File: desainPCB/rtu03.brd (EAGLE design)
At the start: 74.9 x 74.6 mm, 13 parts, among them M1 ARDUINO-PRO-MINI-5.0V, X1 JST-XH-02-PIN-LONG-PAD

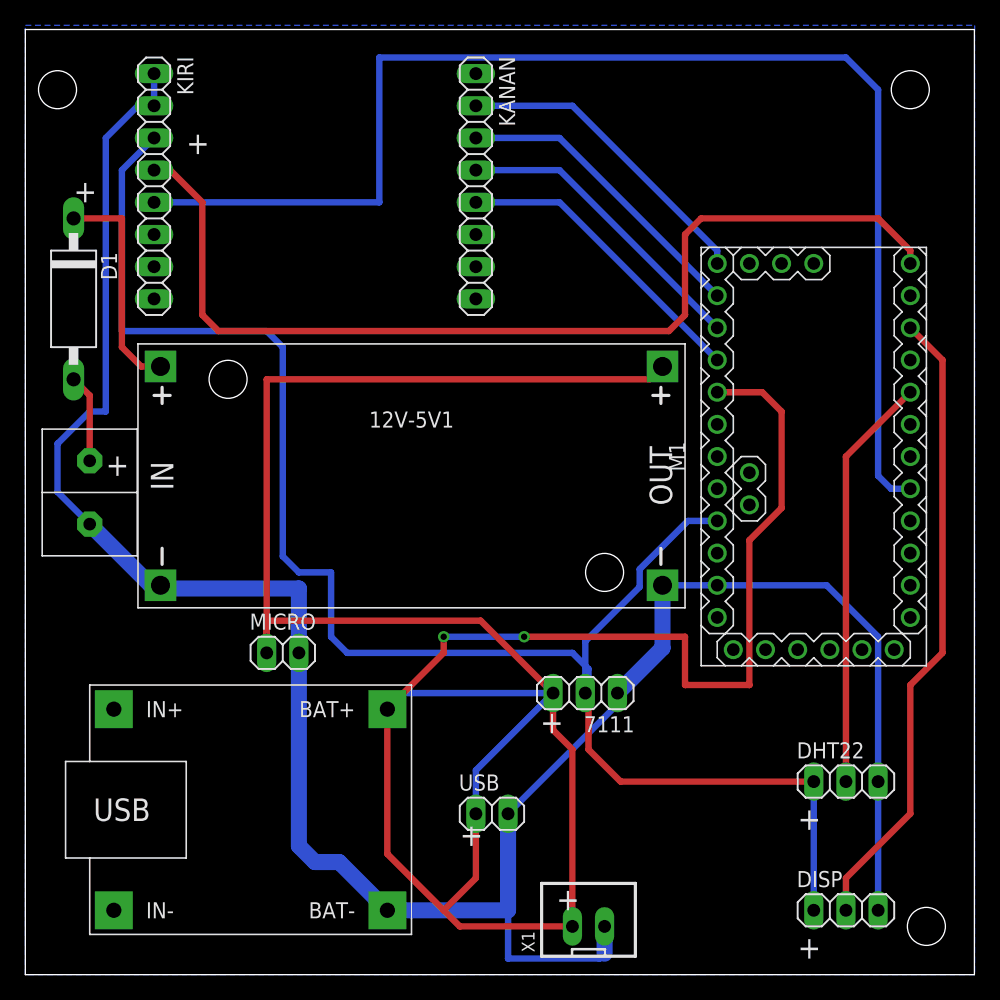
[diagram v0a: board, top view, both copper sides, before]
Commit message: new sensor suhu
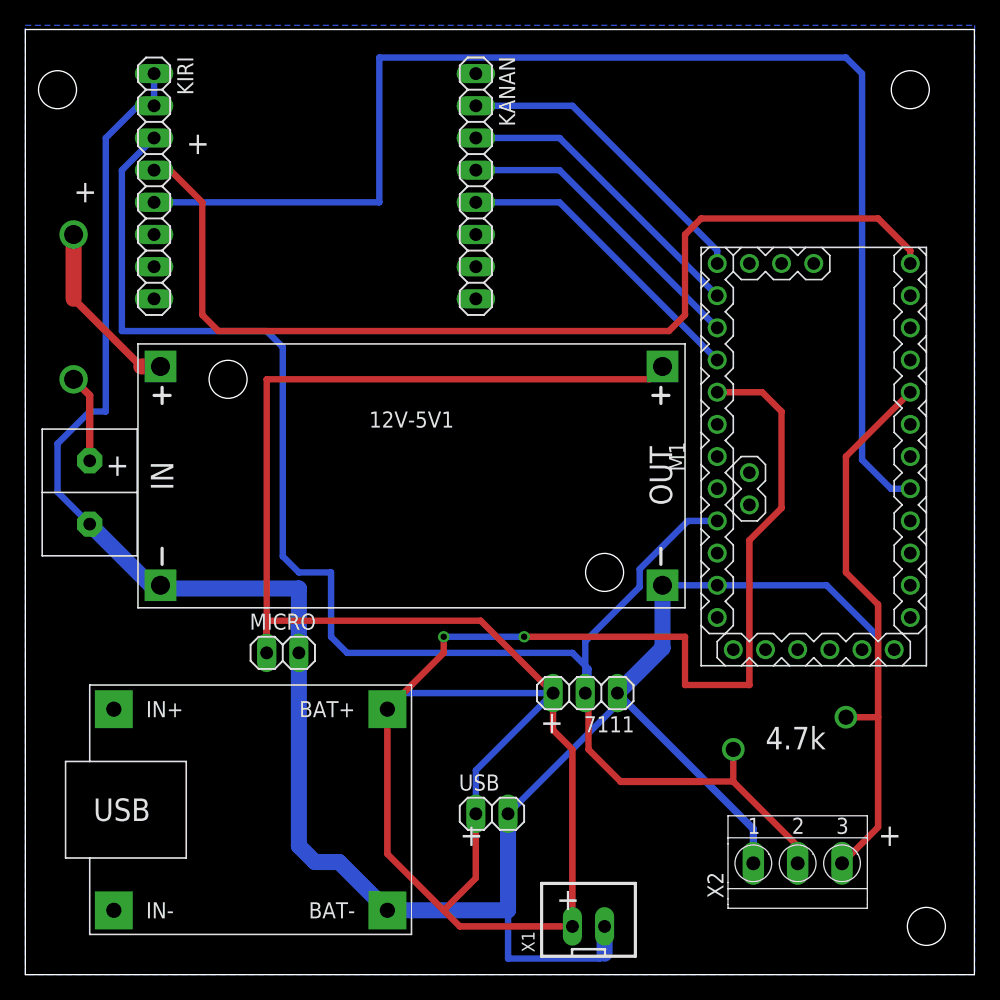
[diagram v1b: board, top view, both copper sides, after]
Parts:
- removed D1: 1N5060GP, diode:DO15-12
- removed DHT22, DISP: (no value), pinhead:1X03
- added X2: TERMINAL-BLOCK-3.5MM-3-PIN-LONG-PAD, Rembrandt Electronics - Terminal Block 3-5mm v1-0:TERMINAL-BLOCK-3-PIN-3.5MM-LONG-PAD
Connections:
- removed net 5: DHT22.2, M1.J7.5
- removed net N$1: D1.A, U$1.P1
- removed net N$2: 12V-5V1.IN+, D1.C
- new net IN+: U$1.P1
- new net OUT+: 12V-5V1.IN+
- net 3V: now also M1.J7.5, X2.2, X2.3; no longer DHT22.1, DISP.1
- net 7: no longer DISP.2
- net GND: now also X2.1; no longer DHT22.3, DISP.3
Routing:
- net 7: track 50.2 -> 0.00 mm
- net 3V: track 131.6 -> 170.4 mm, vias 0 -> 2
- net 5: track 32.8 -> 0.00 mm
- net N$2: track 17.6 -> 0.00 mm
- net OUT+: track 0.00 -> 14.1 mm, vias 0 -> 1
- net N$1: track 6.96 -> 0.00 mm
- net IN+: track 0.00 -> 6.96 mm, vias 0 -> 1
- net GND: track 183.5 -> 179.8 mm
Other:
- board text added: "4.7k"
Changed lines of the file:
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@@
 <text x="40.64" y="19.05" size="1.778" layer="21">+</text>
 <text x="6.35" y="39.37" size="1.778" layer="21">+</text>
-<text x="60.96" y="1.27" size="1.778" layer="21">+</text>
-<text x="60.96" y="11.43" size="1.778" layer="21">+</text>
+<text x="67.31" y="10.16" size="1.778" layer="21">+</text>
 <text x="41.91" y="5.08" size="1.778" layer="21">+</text>
 <text x="3.81" y="60.96" size="1.778" layer="21">+</text>
 <text x="12.7" y="64.77" size="1.778" layer="21">+</text>
+<text x="58.42" y="17.78" size="1.778" layer="21">4.7k</text>
 </plain>
 <attributes>
@@
 <element name="X1" library="Rembrandt Electronics - JST XH Connectors v1-0" package="JST-XH-02-PACKAGE-LONG-PAD" value="JST-XH-02-PIN-LONG-PAD" x="44.45" y="3.81" smashed="yes">
 <attribute name="NAME" x="40.195" y="1.77" size="1.016" layer="25" ratio="10" rot="R90"/>
-<attribute name="VALUE" x="41.1475" y="7.7025" size="1.016" layer="27" ratio="10"/>
 </element>
 <element name="KANAN" library="pinhead" library_urn="urn:adsk.eagle:library:325" package="1X08" package3d_urn="urn:adsk.eagle:package:22409/2" value="" x="35.56" y="62.23" smashed="yes" rot="R270">
@@
 <attribute name="VALUE" x="48.006" y="25.4" size="1.27" layer="27" rot="R180"/>
 </element>
-<element name="DHT22" library="pinhead" library_urn="urn:adsk.eagle:library:325" package="1X03" package3d_urn="urn:adsk.eagle:package:22458/2" value="" x="64.77" y="15.24" smashed="yes">
-<attribute name="NAME" x="60.8838" y="17.0688" size="1.27" layer="25" ratio="10"/>
-<attribute name="POPULARITY" value="92" x="64.77" y="15.24" size="1.778" layer="27" display="off"/>
-<attribute name="VALUE" x="60.96" y="12.065" size="1.27" layer="27"/>
-</element>
-<element name="DISP" library="pinhead" library_urn="urn:adsk.eagle:library:325" package="1X03" package3d_urn="urn:adsk.eagle:package:22458/2" value="" x="64.77" y="5.08" smashed="yes">
-<attribute name="NAME" x="60.8838" y="6.9088" size="1.27" layer="25" ratio="10"/>
-<attribute name="POPULARITY" value="92" x="64.77" y="5.08" size="1.778" layer="27" display="off"/>
-<attribute name="VALUE" x="60.96" y="1.905" size="1.27" layer="27"/>
-</element>
 <element name="U$2" library="diy-modules (1)" package="BATTERY-CHARGER-LI-5V" value="BATTERY-CHARGER-LI-5V" x="17.78" y="12.7" smashed="yes">
 <attribute name="VALUE" x="17.78" y="9.525" size="1.27" layer="27" align="top-center"/>
@@
 <attribute name="VALUE" x="34.29" y="9.525" size="1.27" layer="27"/>
 </element>
-<element name="D1" library="diode" library_urn="urn:adsk.eagle:library:210" package="DO15-12" package3d_urn="urn:adsk.eagle:package:43369/2" value="1N5060GP" x="3.81" y="53.34" smashed="yes" rot="R270">
-<attribute name="NAME" x="5.969" y="57.023" size="1.27" layer="25" ratio="10" rot="R270"/>
-<attribute name="POPULARITY" value="0" x="3.81" y="53.34" size="1.778" layer="27" rot="R270" display="off"/>
-<attribute name="VALUE" x="2.413" y="55.499" size="1.27" layer="27" ratio="10" rot="R270"/>
+<element name="X2" library="Rembrandt Electronics - Terminal Block 3-5mm v1-0" package="TERMINAL-BLOCK-3-PIN-3.5MM-LONG-PAD" value="TERMINAL-BLOCK-3.5MM-3-PIN-LONG-PAD" x="60.96" y="8.89" smashed="yes">
+<attribute name="NAME" x="55.105" y="6.0325" size="1.27" layer="25" rot="R90"/>
 </element>
 </elements>
@@
 <contactref element="KIRI" pad="2"/>
 <contactref element="7111" pad="1"/>
-<contactref element="DHT22" pad="3"/>
-<contactref element="DISP" pad="3"/>
 <contactref element="U$2" pad="BAT-"/>
 <contactref element="MICRO" pad="2"/>
@@
 <wire x1="45.339" y1="1.27" x2="38.1" y2="1.27" width="0.508" layer="16"/>
 <wire x1="38.1" y1="1.27" x2="38.1" y2="5.08" width="0.508" layer="16"/>
-<wire x1="67.31" y1="15.24" x2="67.31" y2="5.08" width="0.508" layer="16"/>
 <wire x1="50.292" y1="30.734" x2="54.61" y2="30.734" width="0.508" layer="16"/>
 <wire x1="54.61" y1="30.734" x2="63.246" y2="30.734" width="0.508" layer="16"/>
 <wire x1="63.246" y1="30.734" x2="67.31" y2="26.67" width="0.508" layer="16"/>
-<wire x1="67.31" y1="26.67" x2="67.31" y2="15.24" width="0.508" layer="16"/>
 <wire x1="10.16" y1="71.12" x2="10.16" y2="68.58" width="0.508" layer="16"/>
 <wire x1="5.08" y1="35.56" x2="2.54" y2="38.1" width="0.508" layer="16"/>
@@
 <vertex x="0" y="0"/>
 </polygon>
+<contactref element="X2" pad="1"/>
+<wire x1="46.736" y1="22.225" x2="57.46" y2="11.501" width="0.58" layer="16"/>
+<wire x1="57.46" y1="11.501" x2="57.46" y2="8.79" width="0.58" layer="16"/>
 </signal>
 <signal name="3V">
 <contactref element="KIRI" pad="3"/>
 <contactref element="7111" pad="2"/>
-<contactref element="DHT22" pad="1"/>
-<contactref element="DISP" pad="1"/>
-<wire x1="62.23" y1="15.24" x2="62.23" y2="5.08" width="0.508" layer="16"/>
 <wire x1="10.16" y1="66.04" x2="7.62" y2="63.5" width="0.508" layer="16"/>
 <wire x1="7.62" y1="63.5" x2="7.62" y2="50.8" width="0.508" layer="16"/>
@@
 <wire x1="44.45" y1="21.971" x2="44.45" y2="17.78" width="0.508" layer="1"/>
 <wire x1="44.45" y1="17.78" x2="46.99" y2="15.24" width="0.508" layer="1"/>
-<wire x1="46.99" y1="15.24" x2="62.23" y2="15.24" width="0.508" layer="1"/>
 <contactref element="M1" pad="J6.4"/>
 <wire x1="44.196" y1="22.225" x2="44.196" y2="26.308625" width="0.508" layer="16"/>
@@
 <wire x1="44.196" y1="26.308625" x2="48.49" y2="30.602625" width="0.508" layer="16"/>
 <wire x1="48.49" y1="30.602625" x2="48.49" y2="32.0067375" width="0.508" layer="16"/>
+<contactref element="X2" pad="3"/>
+<contactref element="X2" pad="2"/>
+<contactref element="M1" pad="J7.5"/>
+<wire x1="69.85" y1="45.974" x2="64.77" y2="40.894" width="0.508" layer="1"/>
+<wire x1="46.99" y1="15.24" x2="53.34" y2="15.24" width="0.58" layer="1"/>
+<wire x1="64.46" y1="8.79" x2="64.665" y2="8.995" width="0.58" layer="1"/>
+<wire x1="64.665" y1="8.995" x2="64.77" y2="9.1" width="0.58" layer="1"/>
+<wire x1="53.34" y1="15.24" x2="55.88" y2="15.24" width="0.508" layer="1"/>
+<wire x1="60.96" y1="10.16" x2="60.96" y2="8.79" width="0.508" layer="1"/>
+<wire x1="55.88" y1="15.24" x2="60.96" y2="10.16" width="0.508" layer="1"/>
+<wire x1="64.77" y1="40.894" x2="64.77" y2="31.75" width="0.508" layer="1"/>
+<wire x1="64.77" y1="31.75" x2="67.31" y2="29.21" width="0.508" layer="1"/>
+<wire x1="67.31" y1="11.64" x2="64.665" y2="8.995" width="0.508" layer="1"/>
+<wire x1="67.31" y1="29.21" x2="67.31" y2="20.32" width="0.508" layer="1"/>
+<wire x1="67.31" y1="20.32" x2="67.31" y2="11.64" width="0.508" layer="1"/>
+<wire x1="67.31" y1="20.32" x2="64.77" y2="20.32" width="0.508" layer="1"/>
+<via x="55.88" y="17.78" extent="1-16" drill="1.2" diameter="1.3" shape="square"/>
+<via x="64.77" y="20.32" extent="1-16" drill="1.2" diameter="1.3" shape="square"/>
+<wire x1="55.88" y1="15.24" x2="55.88" y2="17.78" width="0.508" layer="1"/>
+<wire x1="64.46" y1="8.79" x2="60.96" y2="8.79" width="0" layer="19" extent="1-1"/>
 </signal>
 <signal name="5V">
@@
 <signal name="7">
 <contactref element="M1" pad="J7.3"/>
-<contactref element="DISP" pad="2"/>
-<wire x1="69.85" y1="51.054" x2="72.39" y2="48.514" width="0.508" layer="1"/>
-<wire x1="69.85" y1="22.86" x2="69.85" y2="12.7" width="0.508" layer="1"/>
-<wire x1="69.85" y1="12.7" x2="64.77" y2="7.62" width="0.508" layer="1"/>
-<wire x1="64.77" y1="7.62" x2="64.77" y2="5.08" width="0.508" layer="1"/>
-<wire x1="72.39" y1="48.514" x2="72.39" y2="25.4" width="0.508" layer="1"/>
-<wire x1="72.39" y1="25.4" x2="69.85" y2="22.86" width="0.508" layer="1"/>
 </signal>
 <signal name="N$6">
@@
 <signal name="N$19">
 <contactref element="KANAN" pad="7"/>
-</signal>
-<signal name="5">
-<contactref element="DHT22" pad="2"/>
-<contactref element="M1" pad="J7.5"/>
-<wire x1="69.85" y1="45.974" x2="64.77" y2="40.894" width="0.508" layer="1"/>
-<wire x1="64.77" y1="40.894" x2="64.77" y2="15.24" width="0.508" layer="1"/>
 </signal>
 <signal name="9">
@@
 <wire x1="27.94" y1="60.96" x2="27.94" y2="72.39" width="0.508" layer="16"/>
 <wire x1="27.94" y1="72.39" x2="64.77" y2="72.39" width="0.508" layer="16"/>
-<wire x1="64.77" y1="72.39" x2="67.31" y2="69.85" width="0.508" layer="16"/>
-<wire x1="67.31" y1="39.37" x2="68.326" y2="38.354" width="0.508" layer="16"/>
+<wire x1="64.77" y1="72.39" x2="66.04" y2="71.12" width="0.508" layer="16"/>
+<wire x1="66.04" y1="40.64" x2="68.326" y2="38.354" width="0.508" layer="16"/>
 <wire x1="68.326" y1="38.354" x2="69.85" y2="38.354" width="0.508" layer="16"/>
-<wire x1="67.31" y1="69.85" x2="67.31" y2="39.37" width="0.508" layer="16"/>
+<wire x1="66.04" y1="71.12" x2="66.04" y2="40.64" width="0.508" layer="16"/>
 </signal>
 <signal name="10">
@@
 <wire x1="43.18" y1="68.58" x2="54.61" y2="57.15" width="0.508" layer="16"/>
 </signal>
-<signal name="N$1">
-<contactref element="D1" pad="A"/>
+<signal name="IN+">
 <contactref element="U$1" pad="P1"/>
-<wire x1="3.81" y1="46.99" x2="5.08" y2="45.72" width="0.508" layer="1"/>
-<wire x1="5.08" y1="45.72" x2="5.08" y2="40.56" width="0.508" layer="1"/>
-</signal>
-<signal name="N$2">
+<via x="3.81" y="46.99" extent="1-16" drill="1.5" shape="square"/>
+<wire x1="5.08" y1="45.72" x2="5.08" y2="40.56" width="0.58" layer="1"/>
+<wire x1="3.81" y1="46.99" x2="5.08" y2="45.72" width="0.58" layer="1"/>
+</signal>
+<signal name="OUT+">
 <contactref element="12V-5V1" pad="IN+"/>
-<contactref element="D1" pad="C"/>
-<wire x1="3.81" y1="59.69" x2="7.62" y2="59.69" width="0.508" layer="1"/>
-<wire x1="7.62" y1="59.69" x2="7.62" y2="49.53" width="0.508" layer="1"/>
-<wire x1="7.62" y1="49.53" x2="9.144" y2="48.006" width="0.508" layer="1"/>
-<wire x1="9.144" y1="48.006" x2="10.668" y2="48.006" width="0.508" layer="1"/>
+<via x="3.81" y="58.42" extent="1-16" drill="1.5" shape="square"/>
+<wire x1="10.668" y1="48.006" x2="9.144" y2="48.006" width="1.27" layer="1"/>
+<wire x1="9.144" y1="48.006" x2="3.81" y2="53.34" width="0.58" layer="1"/>
+<wire x1="3.81" y1="53.34" x2="3.81" y2="58.42" width="1.27" layer="1"/>
 </signal>
 </signals>
